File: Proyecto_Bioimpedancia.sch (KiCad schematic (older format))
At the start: 67 parts, among them J1 Jumper, J2 Jumper, J3 Jumper_Calibration, J4 Jumper, J5 Jumper, J6 Jumper, P1 CONN_01X05, P10 CONN_01X03, P11 CONN_01X02, P12 CONN_01X01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

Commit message: PCB-1_Prototipo_1
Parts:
- removed C10, C11: 1uF, Capacitors_SMD:C_0805_HandSoldering, symbol 1uF
- removed C13: 1nF, Capacitors_SMD:C_1206_HandSoldering, symbol 1nF
- removed P1: CONN_01X05, Socket_Strips:Socket_Strip_Straight_1x05_Pitch2.54mm, symbol CONN_01X05
- removed P17: CONN_01X02, Socket_Strips:Socket_Strip_Straight_1x02_Pitch2.54mm, symbol CONN_01X02
- removed R13: 10K, Resistors_SMD:R_0805_HandSoldering, symbol 10K
- removed R14: 78,7K, Resistors_SMD:R_0805_HandSoldering, symbol 78,7K
- removed R15: 140K, Resistors_SMD:R_0805_HandSoldering, symbol 140K
- removed R2, R3, R5, R6: 50K, Resistors_SMD:R_0805_HandSoldering, symbol 50K
- removed U4: ADP3334, Housings_SOIC:SOIC-8_3.9x4.9mm_Pitch1.27mm, symbol ADP3334
- added C10: 0,1uF, Capacitors_SMD:C_0805_HandSoldering, symbol 0,1uF
- added C11: 10uF, Capacitors_SMD:C_0805_HandSoldering, symbol 10uF
- added D3, D4: Z_PROTEC, Diodes_THT:D_DO-41_SOD81_P10.16mm_Horizontal, symbol ZENER_PROTEC
- added P1: PROTECCION_MICRO, Sockets_MOLEX_KK-System:Socket_MOLEX-KK-RM3-96mm_Lock_3pin_straight, symbol CONN_01X03
- added R14, R15: R_PROTEC, Resistors_ThroughHole:R_Axial_DIN0414_L11.9mm_D4.5mm_P20.32mm_Horizontal, symbol R_PROTEC
- added R16, R17: 10K, Resistors_SMD:R_0805_HandSoldering, symbol 10K
- added R2, R3, R5, R6: 20K, Resistors_SMD:R_0805_HandSoldering, symbol 20K
- added U4: LD1117S50TR, TO_SOT_Packages_SMD:SOT-223, symbol LD1117S50TR_FINAL
- added W6: TEST_1P, Measurement_Points:Measurement_Point_Round-TH_Small, symbol TEST_1P
- P10: value CONN_01X03 -> RS-232
- P11: value CONN_01X02 -> SOURCE_2; footprint Socket_Strips:Socket_Strip_Straight_1x02_Pitch2.54mm -> Sockets_MOLEX_KK-System:Socket_MOLEX-KK-RM3-96mm_Lock_2pin_straight
- P12: value CONN_01X01 -> RESET
- P13: value CONN_01X02 -> POWER; footprint Socket_Strips:Socket_Strip_Straight_1x02_Pitch2.54mm -> Sockets_MOLEX_KK-System:Socket_MOLEX-KK-RM3-96mm_Lock_2pin_straight
- P14: value CONN_01X02 -> BIO_OUT1; footprint Socket_Strips:Socket_Strip_Straight_1x02_Pitch2.54mm -> Sockets_MOLEX_KK-System:Socket_MOLEX-KK-RM3-96mm_Lock_2pin_straight
- P15: value CONN_01X01 -> GND_REGULATOR
- P16: value CONN_01X02 -> BIO_OUT2; footprint Socket_Strips:Socket_Strip_Straight_1x02_Pitch2.54mm -> Sockets_MOLEX_KK-System:Socket_MOLEX-KK-RM3-96mm_Lock_2pin_straight
- P2: value CONN_01X08 -> GPIO
- P3: value CONN_01X02 -> SOURCE_3; footprint Socket_Strips:Socket_Strip_Straight_1x02_Pitch2.54mm -> Sockets_MOLEX_KK-System:Socket_MOLEX-KK-RM3-96mm_Lock_2pin_straight
- P4: value CONN_01X04 -> SERIAL_VIRTUAL
- P5: value CONN_01X04 -> ENCODER
- P6: value CONN_01X02 -> I2C_1
- P7: value CONN_01X02 -> I2C_2
- P8: value CONN_01X02 -> SOURCE_1; footprint Socket_Strips:Socket_Strip_Straight_1x02_Pitch2.54mm -> Sockets_MOLEX_KK-System:Socket_MOLEX-KK-RM3-96mm_Lock_2pin_straight
- P9: value CONN_01X04 -> SPI
- renumbered C14 to C13, R16 to R13
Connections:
- net labels added: 5V
- net labels removed: 3V3, D_REG
- wire segments 217 -> 218
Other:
- note added: "Proteccion"
- moved on the sheet: D1, D2, P2, P4, P5, R12, R13

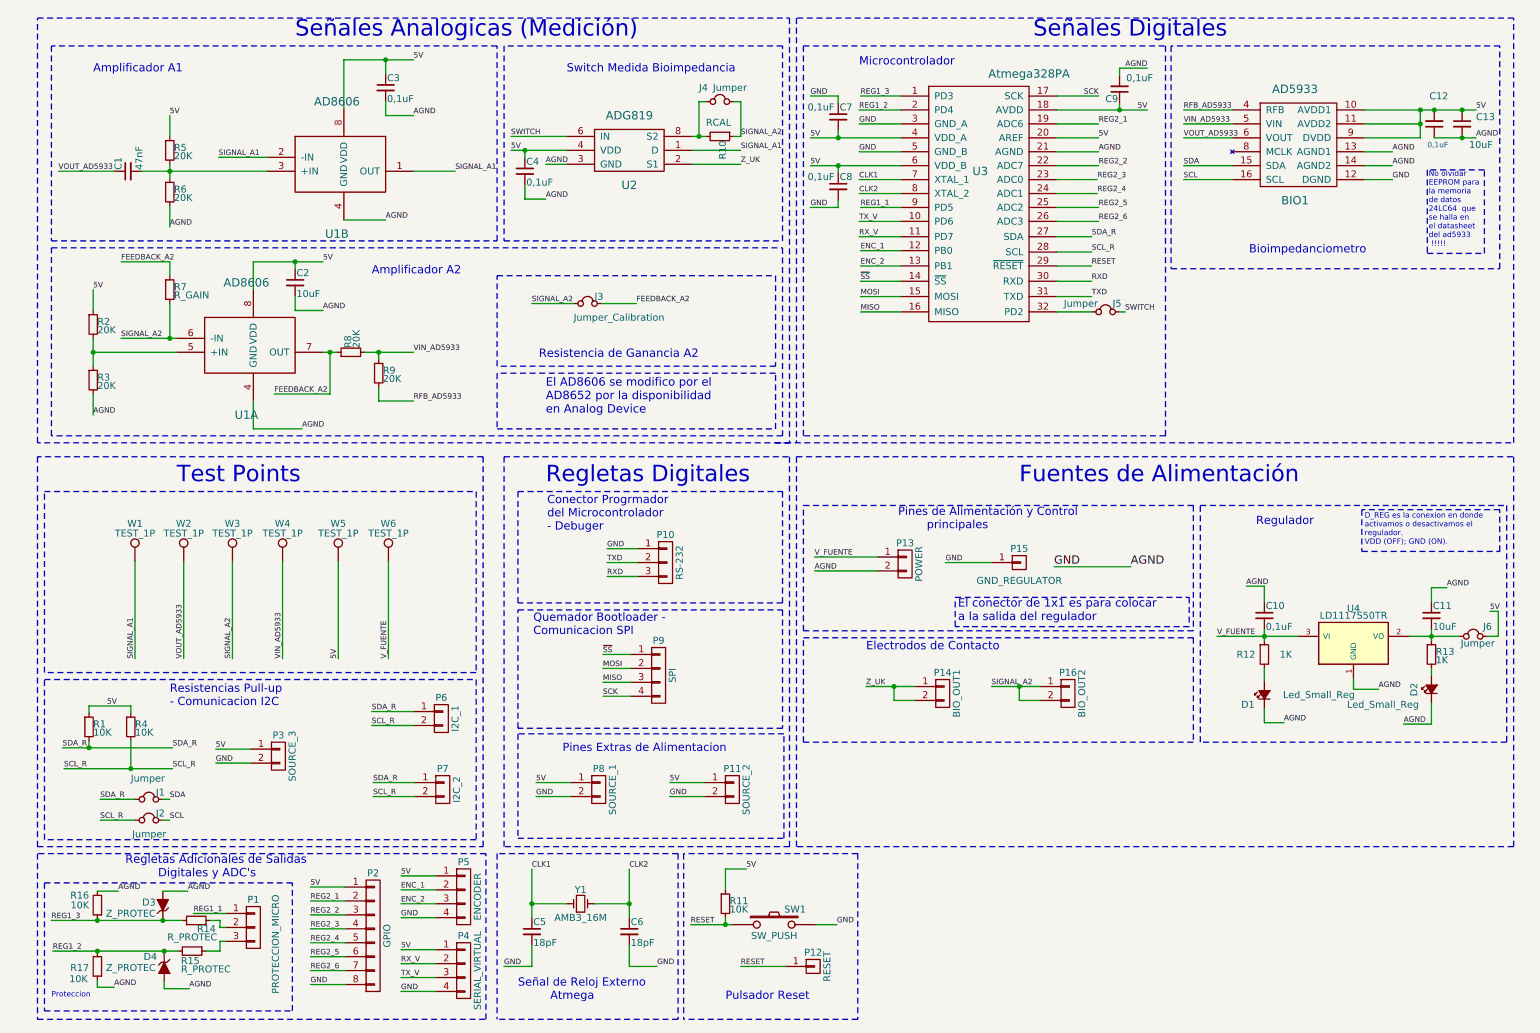
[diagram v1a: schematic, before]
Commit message: Cambio de limites de la PCB
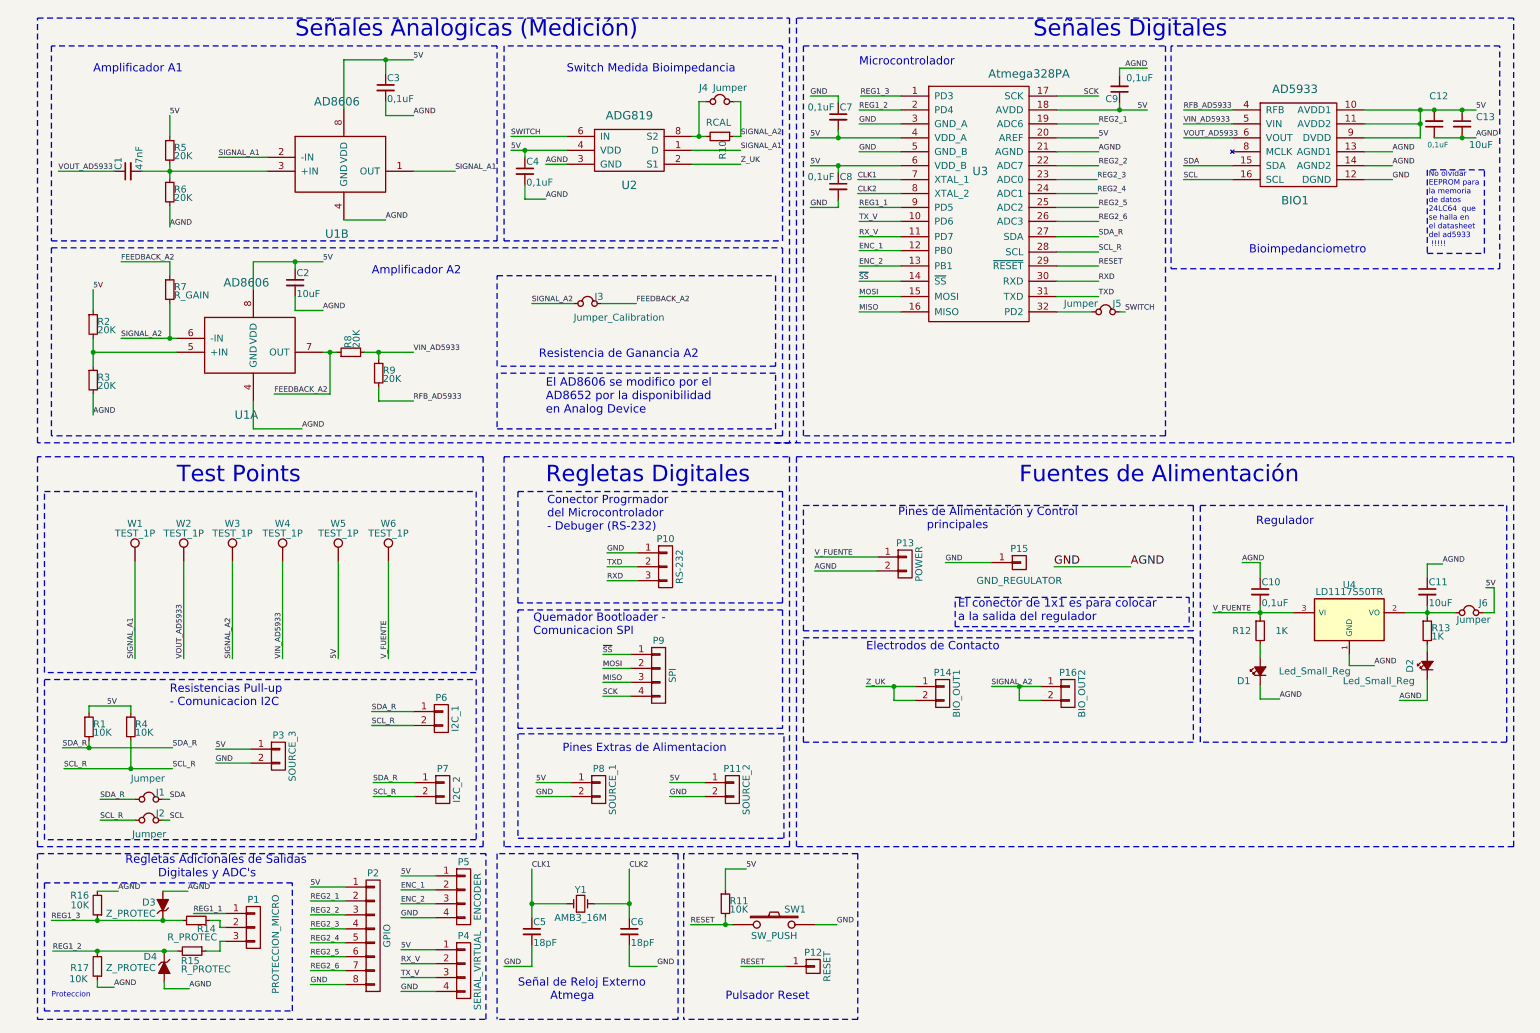
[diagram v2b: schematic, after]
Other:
- note added: "Conector Progrmador \ndel Microcontrolador \n- Debuger (RS-232)"
- note removed: "Conector Progrmador \ndel Microcontrolador \n- Debuger"
- note removed: "D_REG es la conexion en donde \nactivamos o desactivamos el \nregulador.\nVDD (OFF); GND (ON)."
- moved on the sheet: C10, C11, D1, D2, J6, P10, R12, R13, U4

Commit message: Cambio de nombre regleta SD_LAPIZ
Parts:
- P1: value PROTECCION_MICRO -> SD_LAPIZ
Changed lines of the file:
@@
 P 2150 7030
 F 0 "P1" H 2150 7230 50  0000 C CNN
-F 1 "PROTECCION_MICRO" V 2310 6910 50  0000 C CNN
+F 1 "SD_LAPIZ" V 2300 7030 50  0000 C CNN
 F 2 "Sockets_MOLEX_KK-System:Socket_MOLEX-KK-RM3-96mm_Lock_3pin_straight" H 2150 7030 50  0001 C CNN
 F 3 "" H 2150 7030 50  0000 C CNN

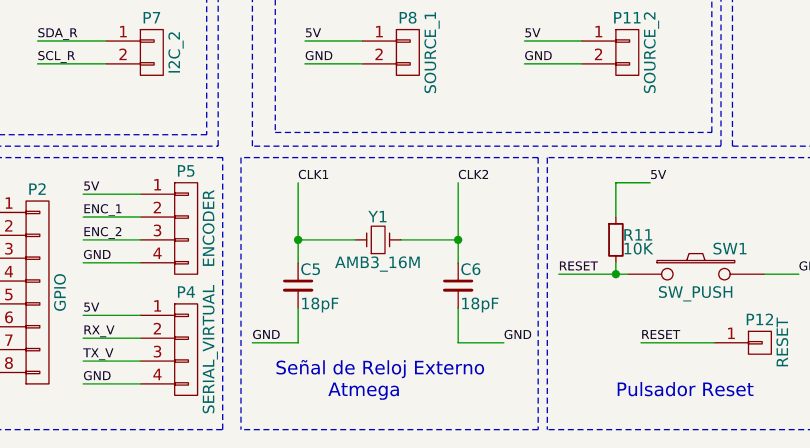
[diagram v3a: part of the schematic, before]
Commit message: Cambio de clock
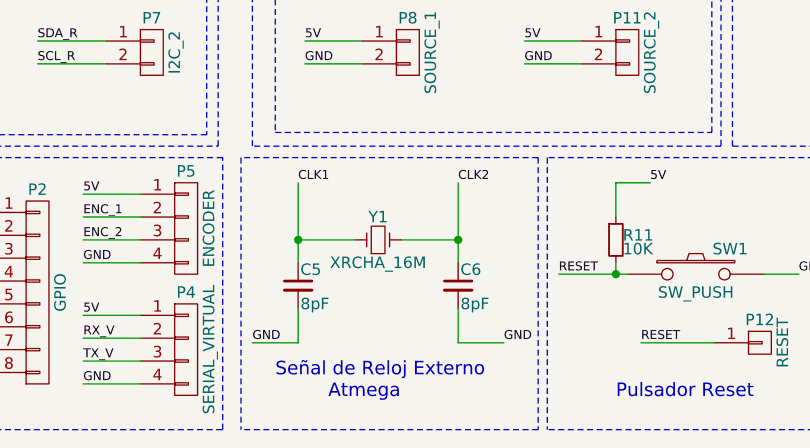
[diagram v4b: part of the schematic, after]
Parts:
- removed C5, C6: 18pF, Capacitors_SMD:C_0805_HandSoldering, symbol 18pF
- removed Y1: AMB3_16M, Crystals:Crystal_SMD_Abracon_ABM3-2pin_5.0x3.2mm_HandSoldering, symbol AMB3_16M
- added C5, C6: 8pF, Capacitors_SMD:C_0805_HandSoldering, symbol 8pF
- added Y1: XRCHA_16M, Huellas:Crystal_SMD_XRCHA_Murata_Serie_W2,5mm_L2,0mm, symbol XRCHA_16M
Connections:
- net AGND: now also C5.2, C6.2
- net CLK1: now also C5.1, Y1.1
- net CLK2: now also C6.1, Y1.2
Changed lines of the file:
@@
-	1    0    0    -1
-$EndComp
-$Comp
-L AMB3_16M Y1
-U 1 1 5912EC72
-P 4500 6860
-F 0 "Y1" H 4500 6960 50  0000 C CNN
-F 1 "AMB3_16M" H 4500 6760 50  0000 C CNN
-F 2 "Crystals:Crystal_SMD_Abracon_ABM3-2pin_5.0x3.2mm_HandSoldering" H 4500 6860 50  0001 C CNN
-F 3 "" H 4500 6860 50  0000 C CNN
-	1    4500 6860
 	1    0    0    -1
 $EndComp
@@
 	1    10580 5150
 	0    -1   -1   0
-$EndComp
-$Comp
-L 18pF C6
-U 1 1 591D60A8
-P 4850 7060
-F 0 "C6" H 4860 7130 50  0000 L CNN
-F 1 "18pF" H 4860 6980 50  0000 L CNN
-F 2 "Capacitors_SMD:C_0805_HandSoldering" H 4760 7030 50  0001 C CNN
-F 3 "" H 4860 7130 50  0000 C CNN
-F 4 "399-1113-2-ND" H 4960 7230 39  0001 C CNN "CAP CER 22PF 50V C0G/NP0 0805"
-	1    4850 7060
-	1    0    0    -1
-$EndComp
-$Comp
-L 18pF C5
-U 1 1 591D65F1
-P 4150 7060
-F 0 "C5" H 4160 7130 50  0000 L CNN
-F 1 "18pF" H 4160 6980 50  0000 L CNN
-F 2 "Capacitors_SMD:C_0805_HandSoldering" H 4060 7030 50  0001 C CNN
-F 3 "" H 4160 7130 50  0000 C CNN
-F 4 "399-1113-2-ND" H 4260 7230 39  0001 C CNN "CAP CER 22PF 50V C0G/NP0 0805"
-	1    4150 7060
-	1    0    0    -1
 $EndComp
 $Comp
@@
 Wire Wire Line
 	1510 7420 1510 7470
+$Comp
+L XRCHA_16M Y1
+U 1 1 59D19E49
+P 4500 6860
+F 0 "Y1" H 4500 6960 50  0000 C CNN
+F 1 "XRCHA_16M" H 4500 6760 50  0000 C CNN
+F 2 "Huellas:Crystal_SMD_XRCHA_Murata_Serie_W2,5mm_L2,0mm" H 4400 6860 50  0001 C CNN
+F 3 "" H 4500 6860 50  0000 C CNN
+	1    4500 6860
+	1    0    0    -1
+$EndComp
+$Comp
+L 8pF C5
+U 1 1 59D19F1A
+P 4150 7060
+F 0 "C5" H 4160 7130 50  0000 L CNN
+F 1 "8pF" H 4160 6980 50  0000 L CNN
+F 2 "Capacitors_SMD:C_0805_HandSoldering" H 4060 7030 50  0001 C CNN
+F 3 "" H 4160 7130 50  0000 C CNN
+F 4 "399-1113-2-ND" H 4260 7230 39  0001 C CNN "CAP CER 22PF 50V C0G/NP0 0805"
+	1    4150 7060
+	1    0    0    -1
+$EndComp
+$Comp
+L 8pF C6
+U 1 1 59D1A05F
+P 4850 7060
+F 0 "C6" H 4860 7130 50  0000 L CNN
+F 1 "8pF" H 4860 6980 50  0000 L CNN
+F 2 "Capacitors_SMD:C_0805_HandSoldering" H 4760 7030 50  0001 C CNN
+F 3 "" H 4860 7130 50  0000 C CNN
+F 4 "399-1113-2-ND" H 4960 7230 39  0001 C CNN "CAP CER 22PF 50V C0G/NP0 0805"
+	1    4850 7060
+	1    0    0    -1
+$EndComp
 $EndSCHEMATC

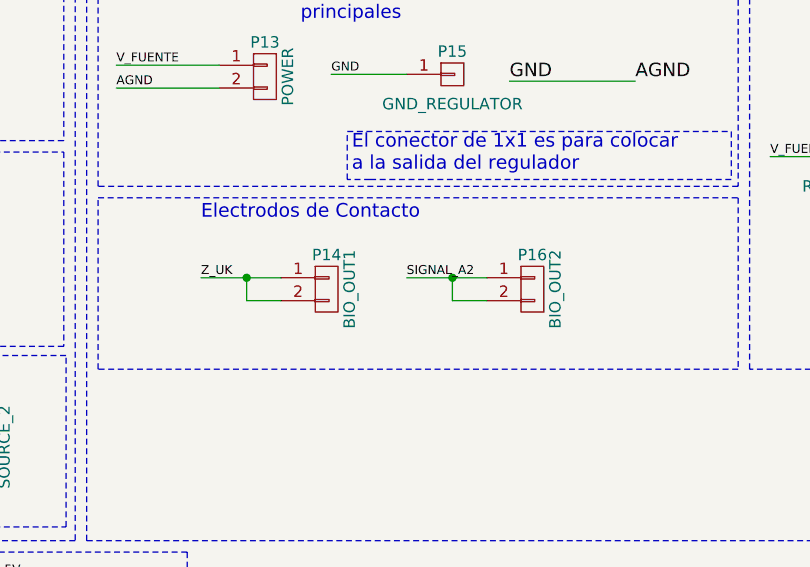
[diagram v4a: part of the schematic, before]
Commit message: Conectores SMA actualizados
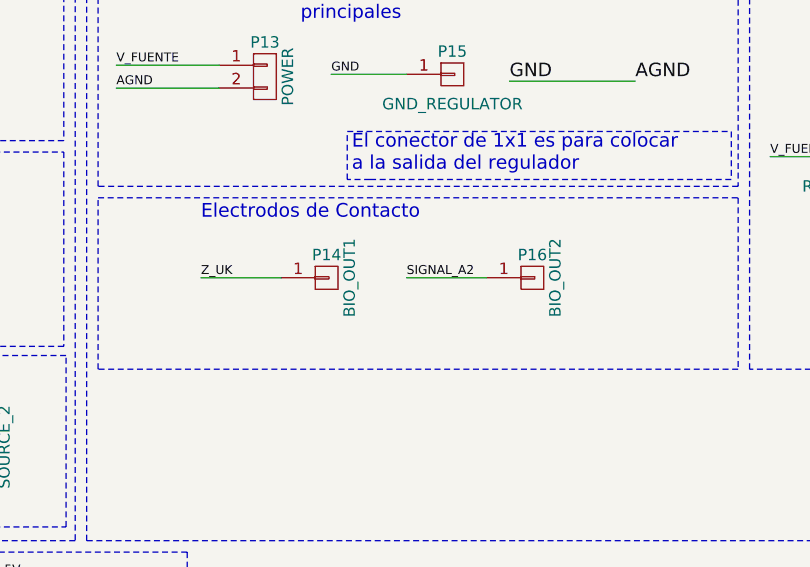
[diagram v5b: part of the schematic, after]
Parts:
- removed P14: BIO_OUT1, Sockets_MOLEX_KK-System:Socket_MOLEX-KK-RM3-96mm_Lock_2pin_straight, symbol CONN_01X02
- removed P16: BIO_OUT2, Sockets_MOLEX_KK-System:Socket_MOLEX-KK-RM3-96mm_Lock_2pin_straight, symbol CONN_01X02
- added P14: BIO_OUT1, Connectors:SMA_THT_Jack_Straight, symbol CONN_01X01
- added P16: BIO_OUT2, Connectors:SMA_THT_Jack_Straight, symbol CONN_01X01
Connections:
- net SIGNAL_A2: now also P16.1 (P1)
- net Z_UK: now also P14.1 (P1)
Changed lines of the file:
@@
 Text Notes 4250 3350 0    60   ~ 0
 El AD8606 se modifico por el \nAD8652 por la disponibilidad \nen Analog Device
-$Comp
-L CONN_01X02 P16
-U 1 1 591D7E68
-P 8000 5350
-F 0 "P16" H 8000 5500 50  0000 C CNN
-F 1 "BIO_OUT2" V 8100 5350 50  0000 C CNN
-F 2 "Sockets_MOLEX_KK-System:Socket_MOLEX-KK-RM3-96mm_Lock_2pin_straight" H 8000 5350 50  0001 C CNN
-F 3 "" H 8000 5350 50  0000 C CNN
-	1    8000 5350
-	1    0    0    -1
-$EndComp
-$Comp
-L CONN_01X02 P14
-U 1 1 591D9B34
-P 7100 5350
-F 0 "P14" H 7100 5500 50  0000 C CNN
-F 1 "BIO_OUT1" V 7200 5350 50  0000 C CNN
-F 2 "Sockets_MOLEX_KK-System:Socket_MOLEX-KK-RM3-96mm_Lock_2pin_straight" H 7100 5350 50  0001 C CNN
-F 3 "" H 7100 5350 50  0000 C CNN
-	1    7100 5350
-	1    0    0    -1
-$EndComp
 Text Notes 1230 6680 0    60   ~ 0
 Regletas Adicionales de Salidas\n         Digitales y ADC's
@@
 Wire Notes Line
 	600  7690 3820 7690
-Connection ~ 7650 5300
-Wire Wire Line
-	7650 5400 7650 5300
-Wire Wire Line
-	7800 5400 7650 5400
-Connection ~ 6750 5300
-Wire Wire Line
-	6750 5400 6750 5300
-Wire Wire Line
-	6900 5400 6750 5400
 Wire Notes Line
 	5900 3050 3900 3050
@@
 	1    0    0    -1
 $EndComp
+$Comp
+L CONN_01X01 P14
+U 1 1 59D2D97F
+P 7100 5300
+F 0 "P14" H 7100 5400 50  0000 C CNN
+F 1 "BIO_OUT1" V 7200 5300 50  0000 C CNN
+F 2 "Connectors:SMA_THT_Jack_Straight" H 7100 5300 50  0001 C CNN
+F 3 "" H 7100 5300 50  0000 C CNN
+	1    7100 5300
+	1    0    0    -1
+$EndComp
+$Comp
+L CONN_01X01 P16
+U 1 1 59D2E997
+P 8000 5300
+F 0 "P16" H 8000 5400 50  0000 C CNN
+F 1 "BIO_OUT2" V 8100 5300 50  0000 C CNN
+F 2 "Connectors:SMA_THT_Jack_Straight" H 8000 5300 50  0001 C CNN
+F 3 "" H 8000 5300 50  0000 C CNN
+	1    8000 5300
+	1    0    0    -1
+$EndComp
